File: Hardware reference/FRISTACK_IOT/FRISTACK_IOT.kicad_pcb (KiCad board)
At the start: 2 copper layers, 51 x 51 mm, 56 parts, among them J2 MEM2075-00-140-01-A, J4 Conn_01x13_Socket, J5 Conn_01x13_Socket, J6 Conn_01x02_Pin, U3 TPS62840DLCR, U4 ESP32-C6-MINI-1-H4, U5 SN65HVD232, Y1 32.768 kHz

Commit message: FRISTACK_IOT_v2
Second version of iot board
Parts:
- removed C27: 100nF, Capacitor_SMD:C_0603_1608Metric
- removed TWAI1: Conn_01x04_Pin, Connector_JST:JST_PH_S4B-PH-K_1x04_P2.00mm_Horizontal
- added C19: 100nF, Capacitor_SMD:C_0603_1608Metric, F.Cu at (176.0, 81.3)
- added G***: LOGO, User_imports:lead_free, B.Cu at (141.4, 105.0)
- added G***: LOGO, iot_footprint:iotlogo, B.Cu at (162.0, 92.9)
- added G***: LOGO, User_imports:fri_logo, B.Cu at (162.0, 77.0)
- added REF**: MountingHole_2mm, MountingHole:MountingHole_2mm, F.Cu at (142.4, 71.4)
- added REF**: MountingHole_2mm, MountingHole:MountingHole_2mm, F.Cu at (142.4, 111.4)
- added REF**: MountingHole_2mm, MountingHole:MountingHole_2mm, F.Cu at (182.4, 71.4)
- added REF**: MountingHole_2mm, MountingHole:MountingHole_2mm, F.Cu at (182.4, 111.4)
- added REF**: KiCad-Logo2_5mm_SilkScreen, Symbol:KiCad-Logo2_5mm_SilkScreen, B.Cu at (161.9, 106.3)
- added REF**: OSHW-Logo_5.7x6mm_SilkScreen, Symbol:OSHW-Logo_5.7x6mm_SilkScreen, B.Cu at (161.9, 113.4)
- moved R18 17.7 mm to (184.3, 106.3), turned to -90 degrees
- moved R17 16.5 mm to (185.9, 106.3), turned to 90 degrees
- moved C5 15.1 mm to (170.8, 105.8), turned to 0 degrees
- moved C6 14.4 mm to (170.8, 104.3), turned to 0 degrees
- moved U3 12.2 mm to (180.8, 104.0), turned to 90 degrees
- moved C3 10.8 mm to (171.5, 115.9), turned to 0 degrees
- moved C4 10.0 mm to (171.5, 114.3), turned to 0 degrees
- moved C2 8.96 mm to (173.4, 112.1)
- moved R7 6.61 mm to (173.4, 109.1), turned to 90 degrees
- moved U1 4.77 mm to (171.3, 110.7), turned to 90 degrees
- moved C8 3.35 mm to (165.1, 94.2)
- moved C1 3.09 mm to (167.5, 94.2)
- moved C11 2.84 mm to (170.2, 98.2), turned to 90 degrees
- moved C7 2.75 mm to (169.4, 110.2), turned to -90 degrees
- moved R10 2.72 mm to (171.8, 98.2), turned to -90 degrees
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- renumbered C22 to C10, C8 to C11, C13 to C12, C14 to C13, C16 to C14, C17 to C15, C20 to C16, C24 to C17, C26 to C18, C10 to C2, C28 to C20, C29 to C21, C30 to C22, C31 to C23, C15 to C3, C18 to C4, C21 to C5, C23 to C6, C9 to C7, C2 to C8, C19 to C9, D5 to D1, J2 to J1, J6 to J2, J4 to J3, J5 to J4, R8 to R1, R9 to R10, R16 to R11, R17 to R12, R18 to R13, R19 to R14, R23 to R15, R21 to R16, R25 to R17, R26 to R18, R27 to R19, R10 to R2, R28 to R20, R24 to R3, R12 to R4, R14 to R5, R5 to R6, R20 to R7, R11 to R8, R22 to R9, U3 to U1, U4 to U2, U5 to U3
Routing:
- net ESP_PWR: track 213.5 -> 188.6 mm, vias 13 -> 8
- net CAN_D: track 27.1 -> 45.1 mm
- net CAN_R: track 26.0 -> 42.2 mm
- net CS: track 25.6 -> 34.2 mm, vias 1 -> 2
- net +5V: track 33.7 -> 41.9 mm, vias 0 -> 2
- net CAN_H: track 26.4 -> 21.5 mm, vias 2 -> 0
- net MOSI: track 45.7 -> 42.3 mm
- net CAN_L: track 25.9 -> 23.0 mm
- net XTAL_32K_N: track 5.84 -> 8.64 mm
- net XTAL_32K_P: track 6.50 -> 8.61 mm
- net GND: track 2.03 -> 0.00 mm, vias 6 -> 208
- net SCK: track 38.6 -> 40.6 mm, vias 2 -> 3
- net USB_P_HD: track 17.6 -> 19.2 mm
- net UART0_TX: track 47.8 -> 46.2 mm
- net Net-(J2-Pin_1): track 4.26 -> 2.93 mm
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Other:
- board text added: "+5V"
- board text added: "ADC_1/IO7"
- board text added: "BOOT/IO40/TDO"
- board text added: "CAN TERM 120Ω"
- board text added: "CAN_H"
- board text added: "CAN_L"
- board text added: "CS/IO10"
- board text added: "ESP_PWR"
- board text added: "GND"
- board text added: "GPIO14"
- board text added: "GPIO17"
- board text added: "GPIO18"
- board text added: "I2S_DIN/IO5"
- board text added: "I2S_DOUT/IO6"
- board text added: "I2S_LRCK/IO4"
- board text added: "MISO/IO11"
- board text added: "MOSI/IO13"
- board text added: "RST/IO39/TCK"
- board text added: "SCK/IO12"
- board text added: "SCL"
- board text added: "SCL/IO9"
- board text added: "SDA"
- board text added: "SDA/IO8"
- board text added: "UART0_RX"
- board text added: "UART0_TX"
- board text added: "USB_N"
- board text added: "USB_P"

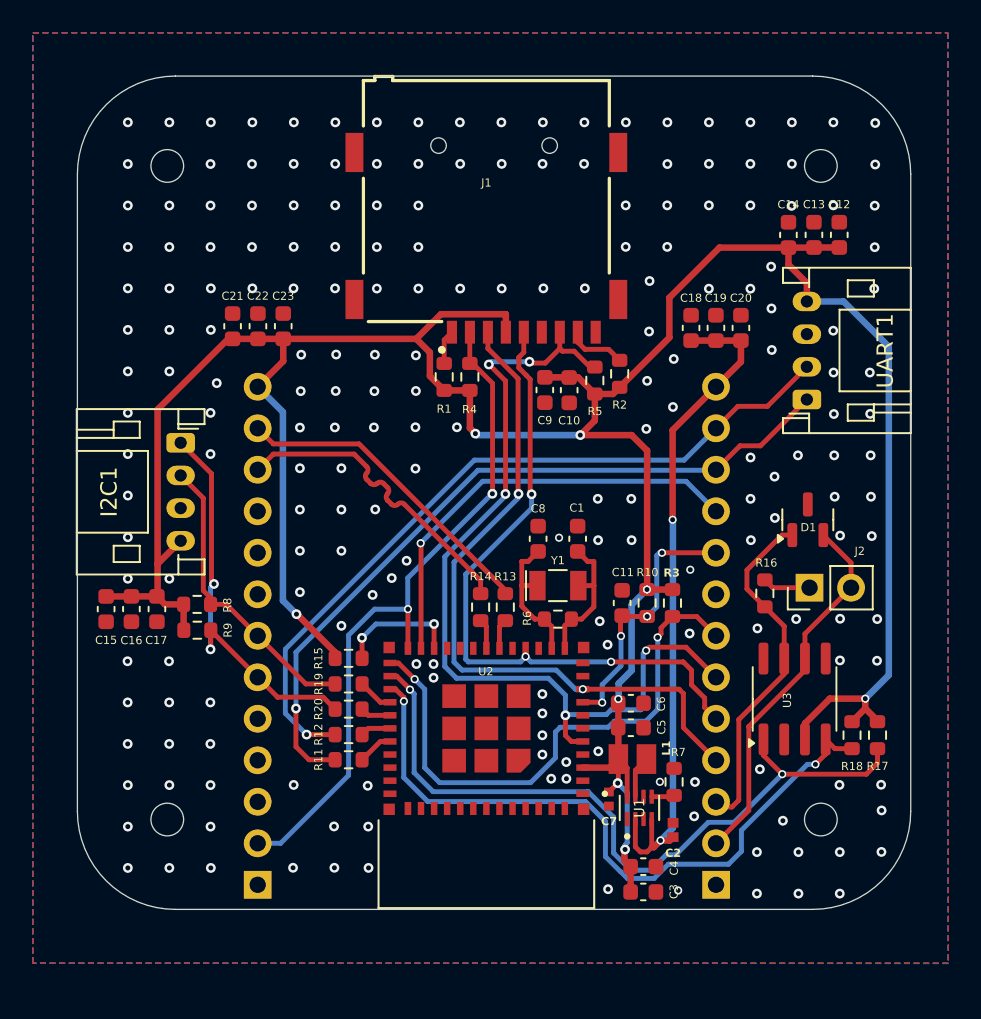
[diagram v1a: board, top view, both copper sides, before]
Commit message: IOT board v3
Switched esp chip with sd card adapter. Replaced 120ohm termination with split termination for TWAI
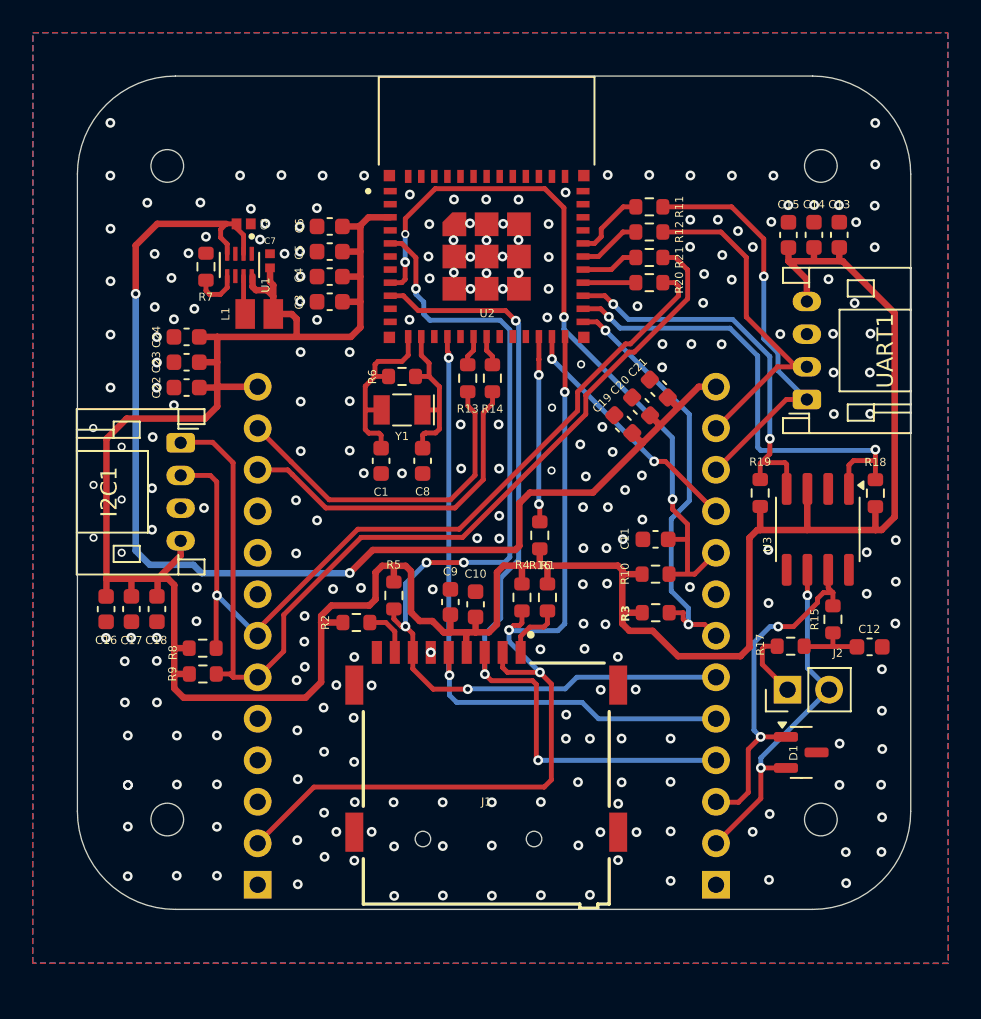
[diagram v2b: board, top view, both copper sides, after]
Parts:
- added C12: 4.7nF, Capacitor_SMD:C_0603_1608Metric, F.Cu at (185.4, 100.9)
- added R15: 60, Resistor_SMD:R_0603_1608Metric, F.Cu at (183.2, 99.2)
- C11: value 1uF -> 0.1uF
- R17: renamed from R16; value 120 -> 60
- moved C2 45.5 mm to (147.1, 75.0), turned to 0 degrees
- moved R7 42.6 mm to (144.8, 77.6)
- moved J1 42.4 mm to (161.5, 112.6), turned to 0 degrees
- moved U1 41.3 mm to (146.8, 77.5), turned to -90 degrees
- moved C3 40.9 mm to (152.4, 79.7), turned to 180 degrees
- moved C4 40.9 mm to (152.4, 78.2), turned to 180 degrees
- moved C7 38.9 mm to (148.7, 77.2), turned to 90 degrees
- moved R11 38.5 mm to (171.9, 73.9), turned to 180 degrees
- moved R12 35.8 mm to (171.9, 75.5), turned to 180 degrees
- moved L1 35.5 mm to (148.0, 80.5), turned to 0 degrees
- moved C6 34.5 mm to (152.4, 75.1), turned to 180 degrees
- moved C5 34.5 mm to (152.4, 76.7), turned to 180 degrees
- moved R21 33.2 mm to (171.9, 77.0), turned to 180 degrees
- moved R20 30.7 mm to (171.9, 78.6), turned to 180 degrees
- moved U2 28.9 mm to (162.0, 77.0), turned to 0 degrees
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- renumbered C12 to C13, C13 to C14, C14 to C15, C15 to C16, C16 to C17, C17 to C18, C18 to C19, C19 to C20, C20 to C21, C21 to C22, C22 to C23, C23 to C24, R15 to R16, R17 to R18, R18 to R19, R19 to R20, R20 to R21
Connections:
- R17 pad 1: CAN_H -> Net-(C12-Pad1)
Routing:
- net SCL: track 24.4 -> 61.0 mm, vias 2 -> 0
- net SDA: track 18.3 -> 53.0 mm, vias 0 -> 1
- net +5V: track 41.9 -> 74.5 mm
- net FLASH_RST: track 16.3 -> 45.8 mm
- net UART0_RX: track 46.6 -> 21.5 mm, vias 1 -> 0
- net UART0_TX: track 46.2 -> 25.3 mm
- net CAN_R: track 42.2 -> 23.9 mm
- net CAN_D: track 45.1 -> 29.8 mm
- net SD_CS: track 42.4 -> 56.1 mm, vias 2 -> 3
- net FLASH_BOOT: track 26.8 -> 15.3 mm, vias 1 -> 2
- net MOSI: track 42.3 -> 51.3 mm, vias 2 -> 3
- net CS: track 34.2 -> 26.3 mm
- net MISO: track 54.3 -> 58.5 mm
- net Net-(C12-Pad1): track 0.00 -> 4.10 mm
- net Net-(U2-IO8): track 7.51 -> 11.4 mm
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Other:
- board text added: "TWAI TERMINATION"
- board text removed: "CAN TERM 120Ω"
